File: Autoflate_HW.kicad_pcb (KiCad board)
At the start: 2 copper layers, 115 x 78 mm, 70 parts, among them J1 JST_XH_3, J10 JST_VH_2, J11 JST_VH_2, J12 JST_XH_3, J13 Header_1, J2 JST_VH_3, J3 JST_XH_2, J4 JST_XH_2, J5 JST_XH_2, J6 JST_XH_2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

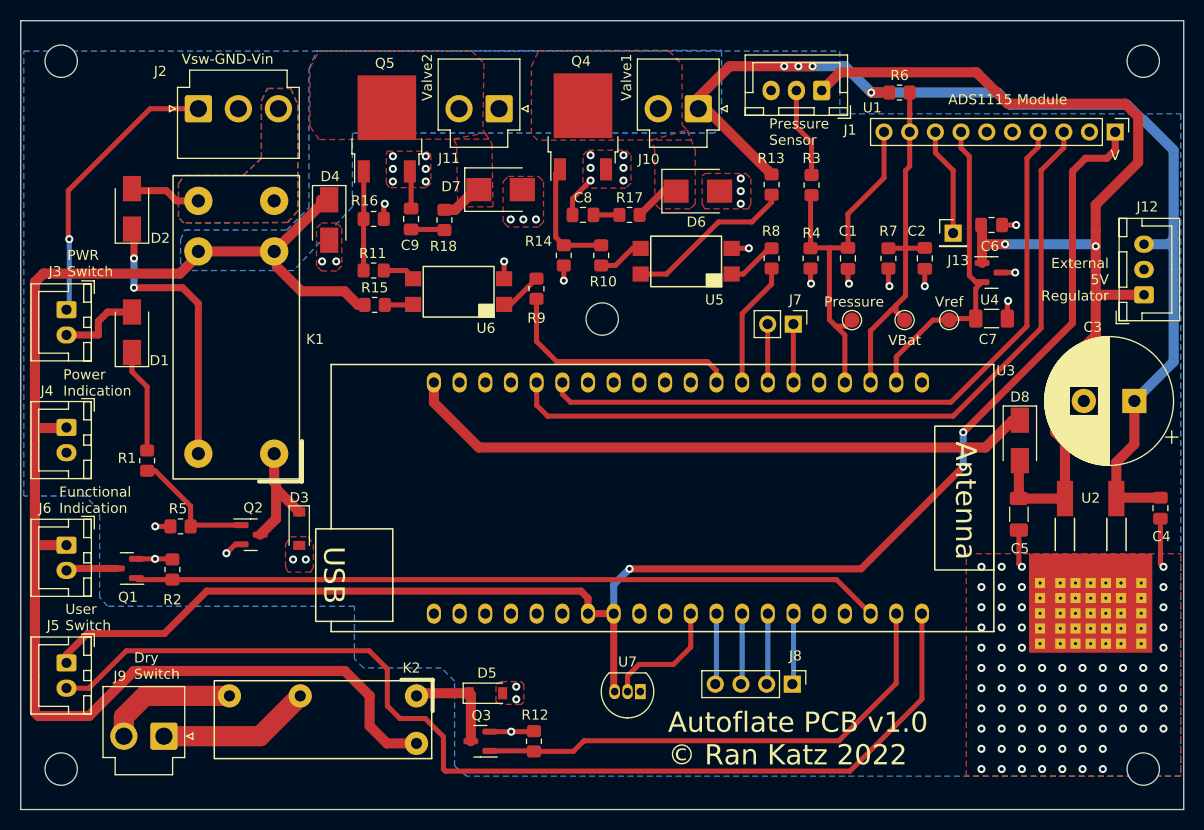
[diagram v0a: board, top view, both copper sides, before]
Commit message: Added Cap on pressure sensor supply
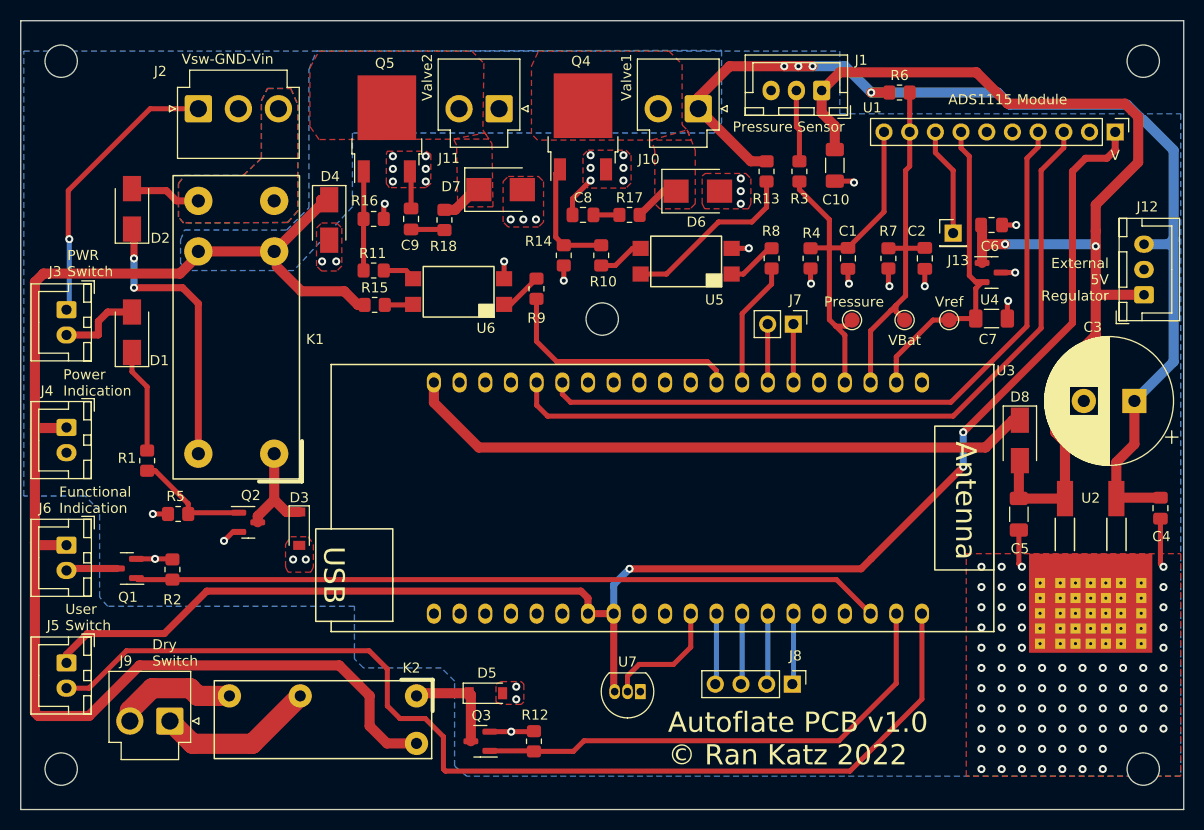
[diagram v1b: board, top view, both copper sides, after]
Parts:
- added C10: 1uF, Capacitor_SMD:C_1206_3216Metric_Pad1.33x1.80mm_HandSolder, F.Cu at (110.5, 41.3)
- moved R3 1.81 mm to (107.0, 41.9)
- moved J9 1.61 mm to (44.8, 96.2)
- moved R13 1.39 mm to (103.8, 41.9)
- moved Q2 1.25 mm to (52.5, 76.6)
- moved R5 1.25 mm to (45.6, 75.8)
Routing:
- net +5V: track 103.8 -> 110.2 mm
- net /Pressure: track 37.7 -> 40.2 mm
- net GND: track 45.4 -> 47.3 mm, vias 113 -> 114
- net Net-(J1-Pad2): track 8.97 -> 7.12 mm
- net Net-(D3-Pad1): track 12.0 -> 10.4 mm
- net Net-(Q2-Pad1): track 12.8 -> 11.5 mm
- net Net-(R13-Pad1): track 16.6 -> 17.7 mm
- net Net-(J9-Pad2): track 13.2 -> 12.1 mm
- net Net-(J9-Pad1): track 15.1 -> 15.8 mm
- net +12V: track 247.8 -> 247.2 mm

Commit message: 4 pin xh
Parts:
- removed J4, J5: JST_XH_2, Connector_JST:JST_XH_B2B-XH-A_1x02_P2.50mm_Vertical
- J3: value JST_XH_2 -> Conn_01x04_Male; footprint Connector_JST:JST_XH_B2B-XH-A_1x02_P2.50mm_Vertical -> Connector_JST:JST_XH_B4B-XH-A_1x04_P2.50mm_Vertical
- J6: value JST_XH_2 -> JST_XH_4; footprint Connector_JST:JST_XH_B2B-XH-A_1x02_P2.50mm_Vertical -> Connector_JST:JST_XH_B4B-XH-A_1x04_P2.50mm_Vertical
- moved J6 22.1 mm to (34.4, 56.8)
- moved J3 17.6 mm to (34.4, 38.0)
- moved D2 11.3 mm to (41.2, 56.9)
- moved D1 9.40 mm to (41.2, 67.2)
- moved R1 4.10 mm to (42.5, 74.6)
- moved R5 2.11 mm to (47.5, 76.6), turned to -90 degrees
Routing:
- net Net-(D1-Pad2): track 8.21 -> 29.4 mm, vias 0 -> 2
- net Net-(J6-Pad2): track 5.12 -> 26.2 mm
- net /User_SW: track 106.5 -> 126.5 mm
- net /VDD3V3: track 149.9 -> 168.1 mm
- net /Vin: track 6.78 -> 21.9 mm
- net Net-(J2-Pad1): track 28.6 -> 14.1 mm, vias 1 -> 0
- net Net-(D2-Pad1): track 27.5 -> 15.9 mm, vias 2 -> 0
- net +12V: track 247.2 -> 239.4 mm
- net Net-(D1-Pad1): track 10.3 -> 4.94 mm
- net Net-(Q2-Pad1): track 11.5 -> 9.08 mm
- net GND: track 47.3 -> 48.1 mm, vias 114 -> 113
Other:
- board text added: "Dry Contact"
- board text removed: "Dry Switch"
